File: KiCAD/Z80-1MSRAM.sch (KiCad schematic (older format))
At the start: 19 parts, among them J1 SBC8080 BUS, U1 7402, U2 74HC573, U3 74HC139, U4 74HC04, U5 74HC00, U6 628128, U7 28C256

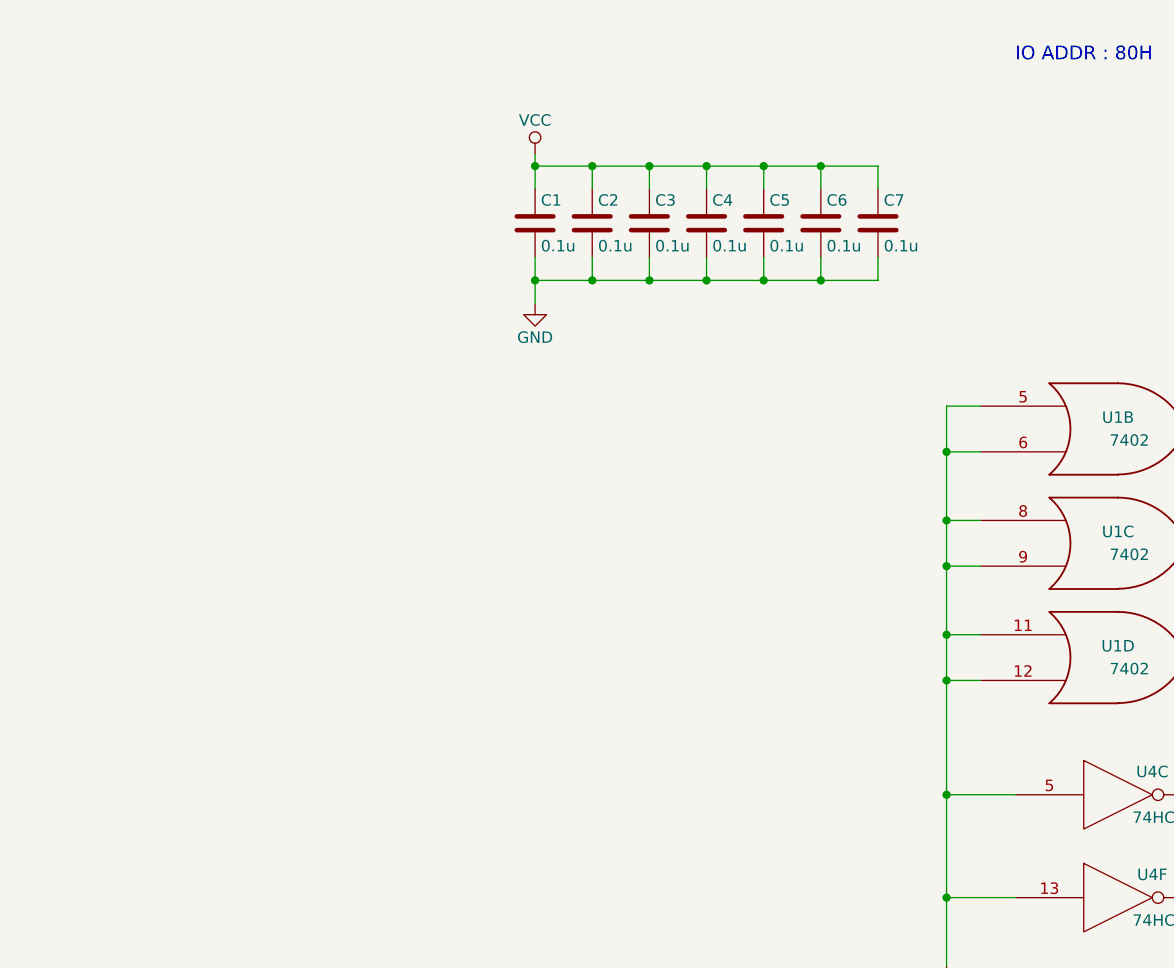
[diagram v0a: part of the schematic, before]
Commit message: 電源部へコンデンサ追加&パターン調整
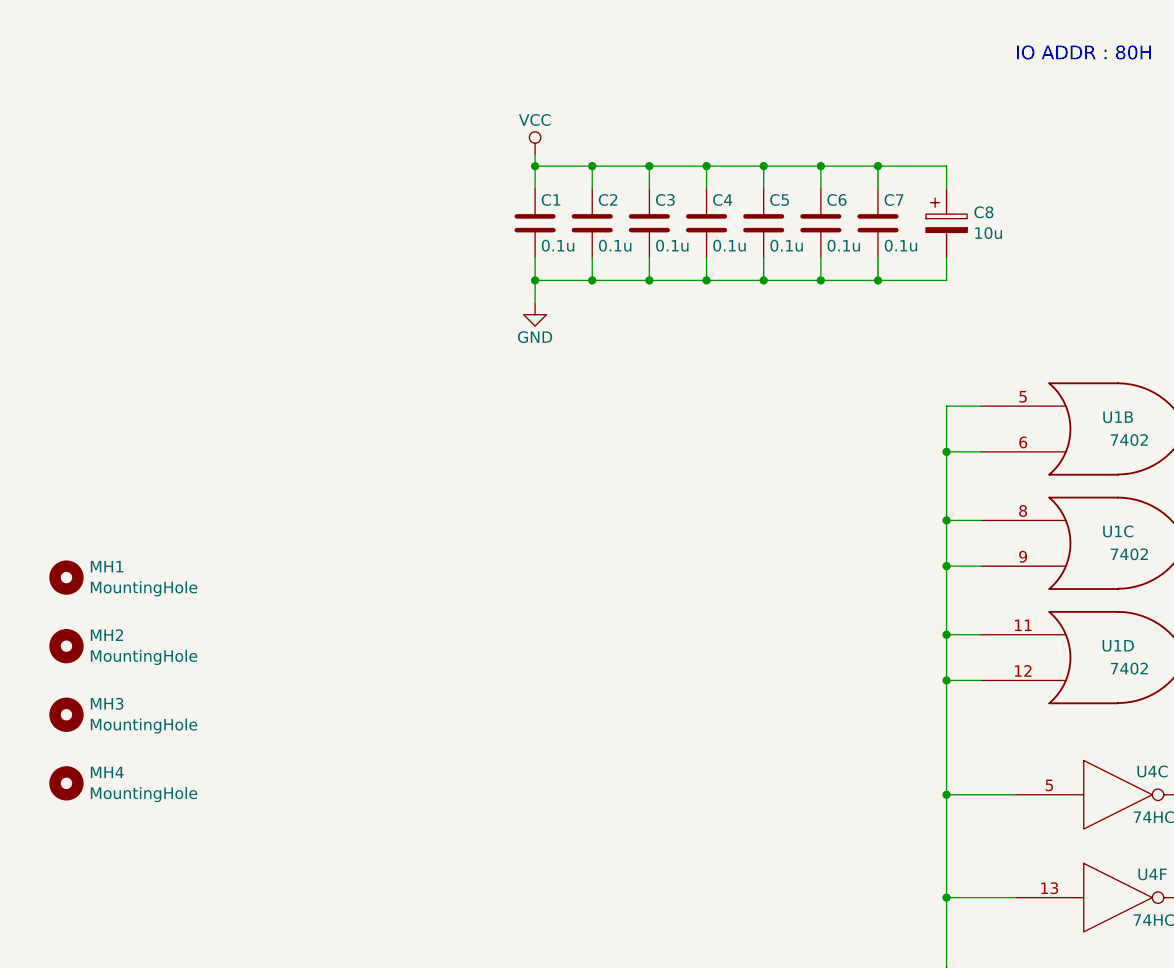
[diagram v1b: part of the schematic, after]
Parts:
- added C8: 10u, Capacitor_THT:CP_Radial_D5.0mm_P2.50mm, symbol Device:CP
- added MH1, MH2, MH3, MH4: MountingHole, MountingHole:MountingHole_3.2mm_M3, symbol Mechanical:MountingHole
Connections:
- wire segments 218 -> 222
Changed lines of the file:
@@
 Wire Wire Line
 	5200 9450 5200 9750
+$Comp
+L Device:CP C8
+U 1 1 5BD00A96
+P 5200 6500
+F 0 "C8" H 5318 6546 50  0000 L CNN
+F 1 "10u" H 5318 6455 50  0000 L CNN
+F 2 "Capacitor_THT:CP_Radial_D5.0mm_P2.50mm" H 5238 6350 50  0001 C CNN
+F 3 "~" H 5200 6500 50  0001 C CNN
+	1    5200 6500
+	1    0    0    -1
+$EndComp
+Wire Wire Line
+	4900 6250 5200 6250
+Wire Wire Line
+	5200 6250 5200 6350
+Connection ~ 4900 6250
+Wire Wire Line
+	4900 6750 5200 6750
+Wire Wire Line
+	5200 6750 5200 6650
 Wire Bus Line
 	6750 2700 6750 3250
@@
 Wire Bus Line
 	12400 2600 12400 7350
+Connection ~ 4900 6750
+$Comp
+L Mechanical:MountingHole MH1
+U 1 1 5BD26C95
+P 1350 8050
+F 0 "MH1" H 1450 8096 50  0000 L CNN
+F 1 "MountingHole" H 1450 8005 50  0000 L CNN
+F 2 "MountingHole:MountingHole_3.2mm_M3" H 1350 8050 50  0001 C CNN
+F 3 "~" H 1350 8050 50  0001 C CNN
+	1    1350 8050
+	1    0    0    -1
+$EndComp
+$Comp
+L Mechanical:MountingHole MH2
+U 1 1 5BD26CF9
+P 1350 8350
+F 0 "MH2" H 1450 8396 50  0000 L CNN
+F 1 "MountingHole" H 1450 8305 50  0000 L CNN
+F 2 "MountingHole:MountingHole_3.2mm_M3" H 1350 8350 50  0001 C CNN
+F 3 "~" H 1350 8350 50  0001 C CNN
+	1    1350 8350
+	1    0    0    -1
+$EndComp
+$Comp
+L Mechanical:MountingHole MH3
+U 1 1 5BD26D50
+P 1350 8650
+F 0 "MH3" H 1450 8696 50  0000 L CNN
+F 1 "MountingHole" H 1450 8605 50  0000 L CNN
+F 2 "MountingHole:MountingHole_3.2mm_M3" H 1350 8650 50  0001 C CNN
+F 3 "~" H 1350 8650 50  0001 C CNN
+	1    1350 8650
+	1    0    0    -1
+$EndComp
+$Comp
+L Mechanical:MountingHole MH4
+U 1 1 5BD26DAA
+P 1350 8950
+F 0 "MH4" H 1450 8996 50  0000 L CNN
+F 1 "MountingHole" H 1450 8905 50  0000 L CNN
+F 2 "MountingHole:MountingHole_3.2mm_M3" H 1350 8950 50  0001 C CNN
+F 3 "~" H 1350 8950 50  0001 C CNN
+	1    1350 8950
+	1    0    0    -1
+$EndComp
 $EndSCHEMATC
